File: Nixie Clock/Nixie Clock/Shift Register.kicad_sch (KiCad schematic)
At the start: 2 parts

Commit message: More Nixie Stuff
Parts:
- removed N?: IN-14, nixies-us_IN-14, symbol nixies-us:IN-14
- removed U?: TPIC6B595N, digikey-footprints:DIP-20_W7.62mm, symbol dk_Logic-Shift-Registers:TPIC6B595N
- added C10, C5, C6, C7, C8, C9: 0.1uF, symbol Device:C
- added U4, U5, U6, U7, U8, U9: TPIC6595N, DIP254P762X508-20, symbol TPIC6595N:TPIC6595N
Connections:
- net +5V: now also C10.1, C5.1, C6.1, C7.1, C8.1, C9.1, U4.2 (VCC), U4.8 (~{SRCLR}), U5.2 (VCC), U5.8 (~{SRCLR}), U6.2 (VCC), U6.8 (~{SRCLR}), U7.2 (VCC), U7.8 (~{SRCLR}), U8.2 (VCC), U8.8 (~{SRCLR}), U9.2 (VCC), U9.8 (~{SRCLR})
- net GND: now also C10.2, C5.2, C6.2, C7.2, C8.2, C9.2, U4.1 (PGND_4), U4.10 (PGND), U4.11 (PGND_3), U4.19 (LGND), U4.20 (PGND_2), U4.9 (~{G}), U5.1 (PGND_4), U5.10 (PGND), U5.11 (PGND_3), U5.19 (LGND), U5.20 (PGND_2), U5.9 (~{G}), U6.1 (PGND_4), U6.10 (PGND), U6.11 (PGND_3), U6.19 (LGND), U6.20 (PGND_2), U6.9 (~{G}), U7.1 (PGND_4), U7.10 (PGND), U7.11 (PGND_3), U7.19 (LGND), U7.20 (PGND_2), U7.9 (~{G}), U8.1 (PGND_4), U8.10 (PGND), U8.11 (PGND_3), U8.19 (LGND), U8.20 (PGND_2), U8.9 (~{G}), U9.1 (PGND_4), U9.10 (PGND), U9.11 (PGND_3), U9.19 (LGND), U9.20 (PGND_2), U9.9 (~{G})
- new net: U8.18 (SER_OUT), U9.3 (SER_IN)
- new net: U6.18 (SER_OUT), U7.3 (SER_IN)
- new net: U5.18 (SER_OUT), U6.3 (SER_IN)
- new net: U4.18 (SER_OUT), U5.3 (SER_IN)
- new net: U7.18 (SER_OUT), U8.3 (SER_IN)
- new net Data Input: U4.3 (SER_IN)
- new net Data Latch: U4.12 (RCK), U5.12 (RCK), U6.12 (RCK), U7.12 (RCK), U8.12 (RCK), U9.12 (RCK)
- new net Shift Clock: U4.13 (SRCK), U5.13 (SRCK), U6.13 (SRCK), U7.13 (SRCK), U8.13 (SRCK), U9.13 (SRCK)
- new net Tube_1_Digit_0: U4.4 (DRAIN0)
- new net Tube_1_Digit_1: U4.5 (DRAIN1)
- new net Tube_1_Digit_2: U4.6 (DRAIN2)
- new net Tube_1_Digit_3: U4.7 (DRAIN3)
- new net Tube_1_Digit_4: U4.14 (DRAIN4)
- new net Tube_1_Digit_5: U4.15 (DRAIN5)
- new net Tube_1_Digit_6: U4.16 (DRAIN6)
- new net Tube_1_Digit_7: U4.17 (DRAIN7)
- new net Tube_1_Digit_8: U5.4 (DRAIN0)
- new net Tube_1_Digit_9: U5.5 (DRAIN1)
- new net Tube_2_Digit_0: U5.6 (DRAIN2)
- new net Tube_2_Digit_1: U5.7 (DRAIN3)
- new net Tube_2_Digit_2: U5.14 (DRAIN4)
- new net Tube_2_Digit_3: U5.15 (DRAIN5)
- new net Tube_2_Digit_4: U5.16 (DRAIN6)
- new net Tube_2_Digit_5: U5.17 (DRAIN7)
- new net Tube_3_Digit_0: U6.4 (DRAIN0)
- new net Tube_3_Digit_1: U6.5 (DRAIN1)
- new net Tube_3_Digit_2: U6.6 (DRAIN2)
- new net Tube_3_Digit_3: U6.7 (DRAIN3)
- new net Tube_3_Digit_4: U6.14 (DRAIN4)
- new net Tube_3_Digit_5: U6.15 (DRAIN5)
- new net Tube_3_Digit_6: U6.16 (DRAIN6)
- new net Tube_3_Digit_7: U6.17 (DRAIN7)
- new net Tube_3_Digit_8: U7.4 (DRAIN0)
- new net Tube_3_Digit_9: U7.5 (DRAIN1)
- new net Tube_4_Digit_0: U7.6 (DRAIN2)
- new net Tube_4_Digit_1: U7.7 (DRAIN3)
- new net Tube_4_Digit_2: U7.14 (DRAIN4)
- new net Tube_4_Digit_3: U7.15 (DRAIN5)
- new net Tube_4_Digit_4: U7.16 (DRAIN6)
- new net Tube_4_Digit_5: U7.17 (DRAIN7)
- new net Tube_5_Digit_0: U8.4 (DRAIN0)
- new net Tube_5_Digit_1: U8.5 (DRAIN1)
- new net Tube_5_Digit_2: U8.6 (DRAIN2)
- new net Tube_5_Digit_3: U8.7 (DRAIN3)
- new net Tube_5_Digit_4: U8.14 (DRAIN4)
- new net Tube_5_Digit_5: U8.15 (DRAIN5)
- new net Tube_5_Digit_6: U8.16 (DRAIN6)
- new net Tube_5_Digit_7: U8.17 (DRAIN7)
- new net Tube_5_Digit_8: U9.4 (DRAIN0)
- new net Tube_5_Digit_9: U9.5 (DRAIN1)
- new net Tube_6_Digit_0: U9.6 (DRAIN2)
- new net Tube_6_Digit_1: U9.7 (DRAIN3)
- new net Tube_6_Digit_2: U9.14 (DRAIN4)
- no-connect marks 0 -> 4

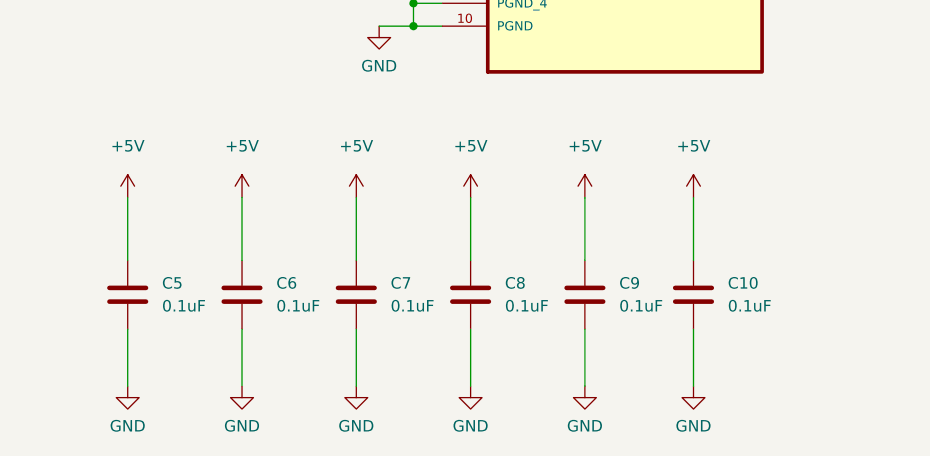
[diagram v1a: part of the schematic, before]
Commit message: Need to add footprints for passives
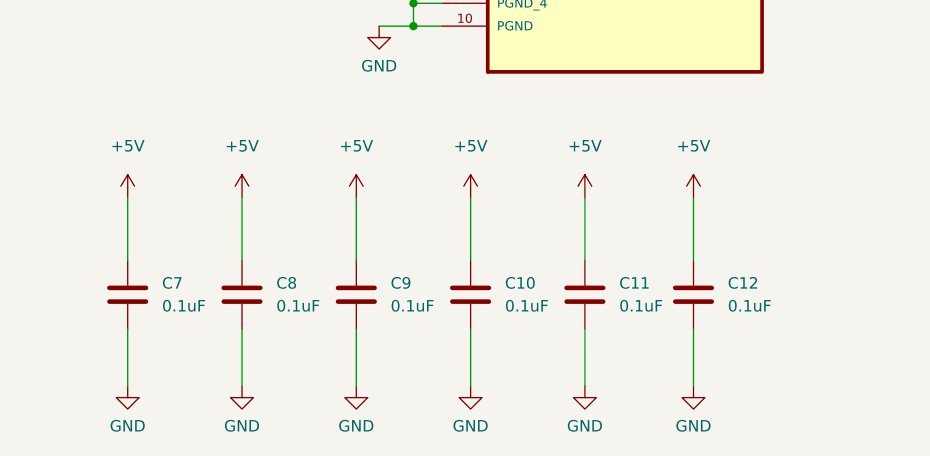
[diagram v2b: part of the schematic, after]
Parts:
- U4, U5, U6, U7, U8, U9: footprint DIP254P762X508-20 -> TPIC6595N:DIP254P762X508-20
- renumbered C8 to C10, C9 to C11, C10 to C12, C5 to C7, C6 to C8, C7 to C9

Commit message: Started Routing
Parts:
- C10, C11, C12, C7, C8, C9: footprint (none) -> Capacitor_THT:C_Rect_L7.0mm_W3.5mm_P5.00mm
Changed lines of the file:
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@@
       (effects (font (size 1.27 1.27)) (justify left))
     )
-    (property "Footprint" "" (id 2) (at 40.3352 183.515 0)
+    (property "Footprint" "Capacitor_THT:C_Rect_L7.0mm_W3.5mm_P5.00mm" (id 2) (at 40.3352 183.515 0)
       (effects (font (size 1.27 1.27)) hide)
     )
@@
       (effects (font (size 1.27 1.27)) (justify left))
     )
-    (property "Footprint" "" (id 2) (at 78.4352 183.515 0)
+    (property "Footprint" "Capacitor_THT:C_Rect_L7.0mm_W3.5mm_P5.00mm" (id 2) (at 78.4352 183.515 0)
       (effects (font (size 1.27 1.27)) hide)
     )
@@
       (effects (font (size 1.27 1.27)) (justify left))
     )
-    (property "Footprint" "" (id 2) (at 65.7352 183.515 0)
+    (property "Footprint" "Capacitor_THT:C_Rect_L7.0mm_W3.5mm_P5.00mm" (id 2) (at 65.7352 183.515 0)
       (effects (font (size 1.27 1.27)) hide)
     )
@@
       (effects (font (size 1.27 1.27)) (justify left))
     )
-    (property "Footprint" "" (id 2) (at 90.5002 183.515 0)
+    (property "Footprint" "Capacitor_THT:C_Rect_L7.0mm_W3.5mm_P5.00mm" (id 2) (at 90.5002 183.515 0)
       (effects (font (size 1.27 1.27)) hide)
     )
@@
       (effects (font (size 1.27 1.27)) (justify left))
     )
-    (property "Footprint" "" (id 2) (at 27.6352 183.515 0)
+    (property "Footprint" "Capacitor_THT:C_Rect_L7.0mm_W3.5mm_P5.00mm" (id 2) (at 27.6352 183.515 0)
       (effects (font (size 1.27 1.27)) hide)
     )
@@
       (effects (font (size 1.27 1.27)) (justify left))
     )
-    (property "Footprint" "" (id 2) (at 53.0352 183.515 0)
-      (effects (font (size 1.27 1.27)) hide)
-    )
+    (property "Footprint" "Capacitor_THT:C_Rect_L7.0mm_W3.5mm_P5.00mm" (id 2) (at 53.0352 183.515 0)
+      (effects (font (size 1.27 1.27)) hide)
+    )

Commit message: Nixie
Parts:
- C10, C11, C12, C7, C8, C9: value 0.1uF -> (none); footprint Capacitor_THT:C_Rect_L7.0mm_W3.5mm_P5.00mm -> (none)
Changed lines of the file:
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@@
       (effects (font (size 1.27 1.27)) (justify left))
     )
-    (property "Value" "0.1uF" (id 1) (at 43.18 180.9749 0)
-      (effects (font (size 1.27 1.27)) (justify left))
-    )
-    (property "Footprint" "Capacitor_THT:C_Rect_L7.0mm_W3.5mm_P5.00mm" (id 2) (at 40.3352 183.515 0)
+    (property "Value" "" (id 1) (at 43.18 180.9749 0)
+      (effects (font (size 1.27 1.27)) (justify left))
+    )
+    (property "Footprint" "" (id 2) (at 40.3352 183.515 0)
       (effects (font (size 1.27 1.27)) hide)
     )
@@
       (effects (font (size 1.27 1.27)) (justify left))
     )
-    (property "Value" "0.1uF" (id 1) (at 81.28 180.9749 0)
-      (effects (font (size 1.27 1.27)) (justify left))
-    )
-    (property "Footprint" "Capacitor_THT:C_Rect_L7.0mm_W3.5mm_P5.00mm" (id 2) (at 78.4352 183.515 0)
+    (property "Value" "" (id 1) (at 81.28 180.9749 0)
+      (effects (font (size 1.27 1.27)) (justify left))
+    )
+    (property "Footprint" "" (id 2) (at 78.4352 183.515 0)
       (effects (font (size 1.27 1.27)) hide)
     )
@@
       (effects (font (size 1.27 1.27)) (justify left))
     )
-    (property "Value" "0.1uF" (id 1) (at 68.58 180.9749 0)
-      (effects (font (size 1.27 1.27)) (justify left))
-    )
-    (property "Footprint" "Capacitor_THT:C_Rect_L7.0mm_W3.5mm_P5.00mm" (id 2) (at 65.7352 183.515 0)
+    (property "Value" "" (id 1) (at 68.58 180.9749 0)
+      (effects (font (size 1.27 1.27)) (justify left))
+    )
+    (property "Footprint" "" (id 2) (at 65.7352 183.515 0)
       (effects (font (size 1.27 1.27)) hide)
     )
@@
       (effects (font (size 1.27 1.27)) (justify left))
     )
-    (property "Value" "0.1uF" (id 1) (at 93.345 180.9749 0)
-      (effects (font (size 1.27 1.27)) (justify left))
-    )
-    (property "Footprint" "Capacitor_THT:C_Rect_L7.0mm_W3.5mm_P5.00mm" (id 2) (at 90.5002 183.515 0)
+    (property "Value" "" (id 1) (at 93.345 180.9749 0)
+      (effects (font (size 1.27 1.27)) (justify left))
+    )
+    (property "Footprint" "" (id 2) (at 90.5002 183.515 0)
       (effects (font (size 1.27 1.27)) hide)
     )
@@
       (effects (font (size 1.27 1.27)) (justify left))
     )
-    (property "Value" "0.1uF" (id 1) (at 30.48 180.9749 0)
-      (effects (font (size 1.27 1.27)) (justify left))
-    )
-    (property "Footprint" "Capacitor_THT:C_Rect_L7.0mm_W3.5mm_P5.00mm" (id 2) (at 27.6352 183.515 0)
+    (property "Value" "" (id 1) (at 30.48 180.9749 0)
+      (effects (font (size 1.27 1.27)) (justify left))
+    )
+    (property "Footprint" "" (id 2) (at 27.6352 183.515 0)
       (effects (font (size 1.27 1.27)) hide)
     )
@@
       (effects (font (size 1.27 1.27)) (justify left))
     )
-    (property "Value" "0.1uF" (id 1) (at 55.88 180.9749 0)
-      (effects (font (size 1.27 1.27)) (justify left))
-    )
-    (property "Footprint" "Capacitor_THT:C_Rect_L7.0mm_W3.5mm_P5.00mm" (id 2) (at 53.0352 183.515 0)
-      (effects (font (size 1.27 1.27)) hide)
-    )
+    (property "Value" "" (id 1) (at 55.88 180.9749 0)
+      (effects (font (size 1.27 1.27)) (justify left))
+    )
+    (property "Footprint" "" (id 2) (at 53.0352 183.515 0)
+      (effects (font (size 1.27 1.27)) hide)
+    )

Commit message: Added additional parts
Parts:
- C10, C11, C12, C7, C8, C9: value (none) -> 0.1uF; footprint (none) -> Capacitor_THT:CP_Radial_D4.0mm_P1.50mm
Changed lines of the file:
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@@
       (effects (font (size 1.27 1.27)) (justify left))
     )
-    (property "Value" "" (id 1) (at 43.18 180.9749 0)
-      (effects (font (size 1.27 1.27)) (justify left))
-    )
-    (property "Footprint" "" (id 2) (at 40.3352 183.515 0)
+    (property "Value" "0.1uF" (id 1) (at 43.18 180.9749 0)
+      (effects (font (size 1.27 1.27)) (justify left))
+    )
+    (property "Footprint" "Capacitor_THT:CP_Radial_D4.0mm_P1.50mm" (id 2) (at 40.3352 183.515 0)
       (effects (font (size 1.27 1.27)) hide)
     )
@@
       (effects (font (size 1.27 1.27)) (justify left))
     )
-    (property "Value" "" (id 1) (at 81.28 180.9749 0)
-      (effects (font (size 1.27 1.27)) (justify left))
-    )
-    (property "Footprint" "" (id 2) (at 78.4352 183.515 0)
+    (property "Value" "0.1uF" (id 1) (at 81.28 180.9749 0)
+      (effects (font (size 1.27 1.27)) (justify left))
+    )
+    (property "Footprint" "Capacitor_THT:CP_Radial_D4.0mm_P1.50mm" (id 2) (at 78.4352 183.515 0)
       (effects (font (size 1.27 1.27)) hide)
     )
@@
       (effects (font (size 1.27 1.27)) (justify left))
     )
-    (property "Value" "" (id 1) (at 68.58 180.9749 0)
-      (effects (font (size 1.27 1.27)) (justify left))
-    )
-    (property "Footprint" "" (id 2) (at 65.7352 183.515 0)
+    (property "Value" "0.1uF" (id 1) (at 68.58 180.9749 0)
+      (effects (font (size 1.27 1.27)) (justify left))
+    )
+    (property "Footprint" "Capacitor_THT:CP_Radial_D4.0mm_P1.50mm" (id 2) (at 65.7352 183.515 0)
       (effects (font (size 1.27 1.27)) hide)
     )
@@
       (effects (font (size 1.27 1.27)) (justify left))
     )
-    (property "Value" "" (id 1) (at 93.345 180.9749 0)
-      (effects (font (size 1.27 1.27)) (justify left))
-    )
-    (property "Footprint" "" (id 2) (at 90.5002 183.515 0)
+    (property "Value" "0.1uF" (id 1) (at 93.345 180.9749 0)
+      (effects (font (size 1.27 1.27)) (justify left))
+    )
+    (property "Footprint" "Capacitor_THT:CP_Radial_D4.0mm_P1.50mm" (id 2) (at 90.5002 183.515 0)
       (effects (font (size 1.27 1.27)) hide)
     )
@@
       (effects (font (size 1.27 1.27)) (justify left))
     )
-    (property "Value" "" (id 1) (at 30.48 180.9749 0)
-      (effects (font (size 1.27 1.27)) (justify left))
-    )
-    (property "Footprint" "" (id 2) (at 27.6352 183.515 0)
+    (property "Value" "0.1uF" (id 1) (at 30.48 180.9749 0)
+      (effects (font (size 1.27 1.27)) (justify left))
+    )
+    (property "Footprint" "Capacitor_THT:CP_Radial_D4.0mm_P1.50mm" (id 2) (at 27.6352 183.515 0)
       (effects (font (size 1.27 1.27)) hide)
     )
@@
       (effects (font (size 1.27 1.27)) (justify left))
     )
-    (property "Value" "" (id 1) (at 55.88 180.9749 0)
-      (effects (font (size 1.27 1.27)) (justify left))
-    )
-    (property "Footprint" "" (id 2) (at 53.0352 183.515 0)
-      (effects (font (size 1.27 1.27)) hide)
-    )
+    (property "Value" "0.1uF" (id 1) (at 55.88 180.9749 0)
+      (effects (font (size 1.27 1.27)) (justify left))
+    )
+    (property "Footprint" "Capacitor_THT:CP_Radial_D4.0mm_P1.50mm" (id 2) (at 53.0352 183.515 0)
+      (effects (font (size 1.27 1.27)) hide)
+    )
